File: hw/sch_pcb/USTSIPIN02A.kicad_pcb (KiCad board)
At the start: 2 copper layers, 90.9 x 50.3 mm, 119 parts, among them J1 SM08B-GHS-TB, J2 SD_Card-FPS009-4200-0, J22 HEADER_2x03, J3 SM06B-GHS-TB, J4 USBC_USB4105-GF-A, M1 HOLE, M2 HOLE, M3 HOLE, M4 HOLE, M8 BMI-S-204-F, Q1 BF862, U1 OPA2314, U10 ATMEGA1284P-AU, U11 PCF85263A, U12 MIC5504-3.3YM5, U2 OPA2314, U3 ISL21080DIH312Z-TK 1V25, U4 TS7211, U5 TS5A4594, U6 AT24CS64-SSHM, U7 USBLC6-2SC6, U8 TPS613222ADBV, U9 FT231XQ, Y1 16MHz, Y2 ABS07-120-32.768KHZ-T

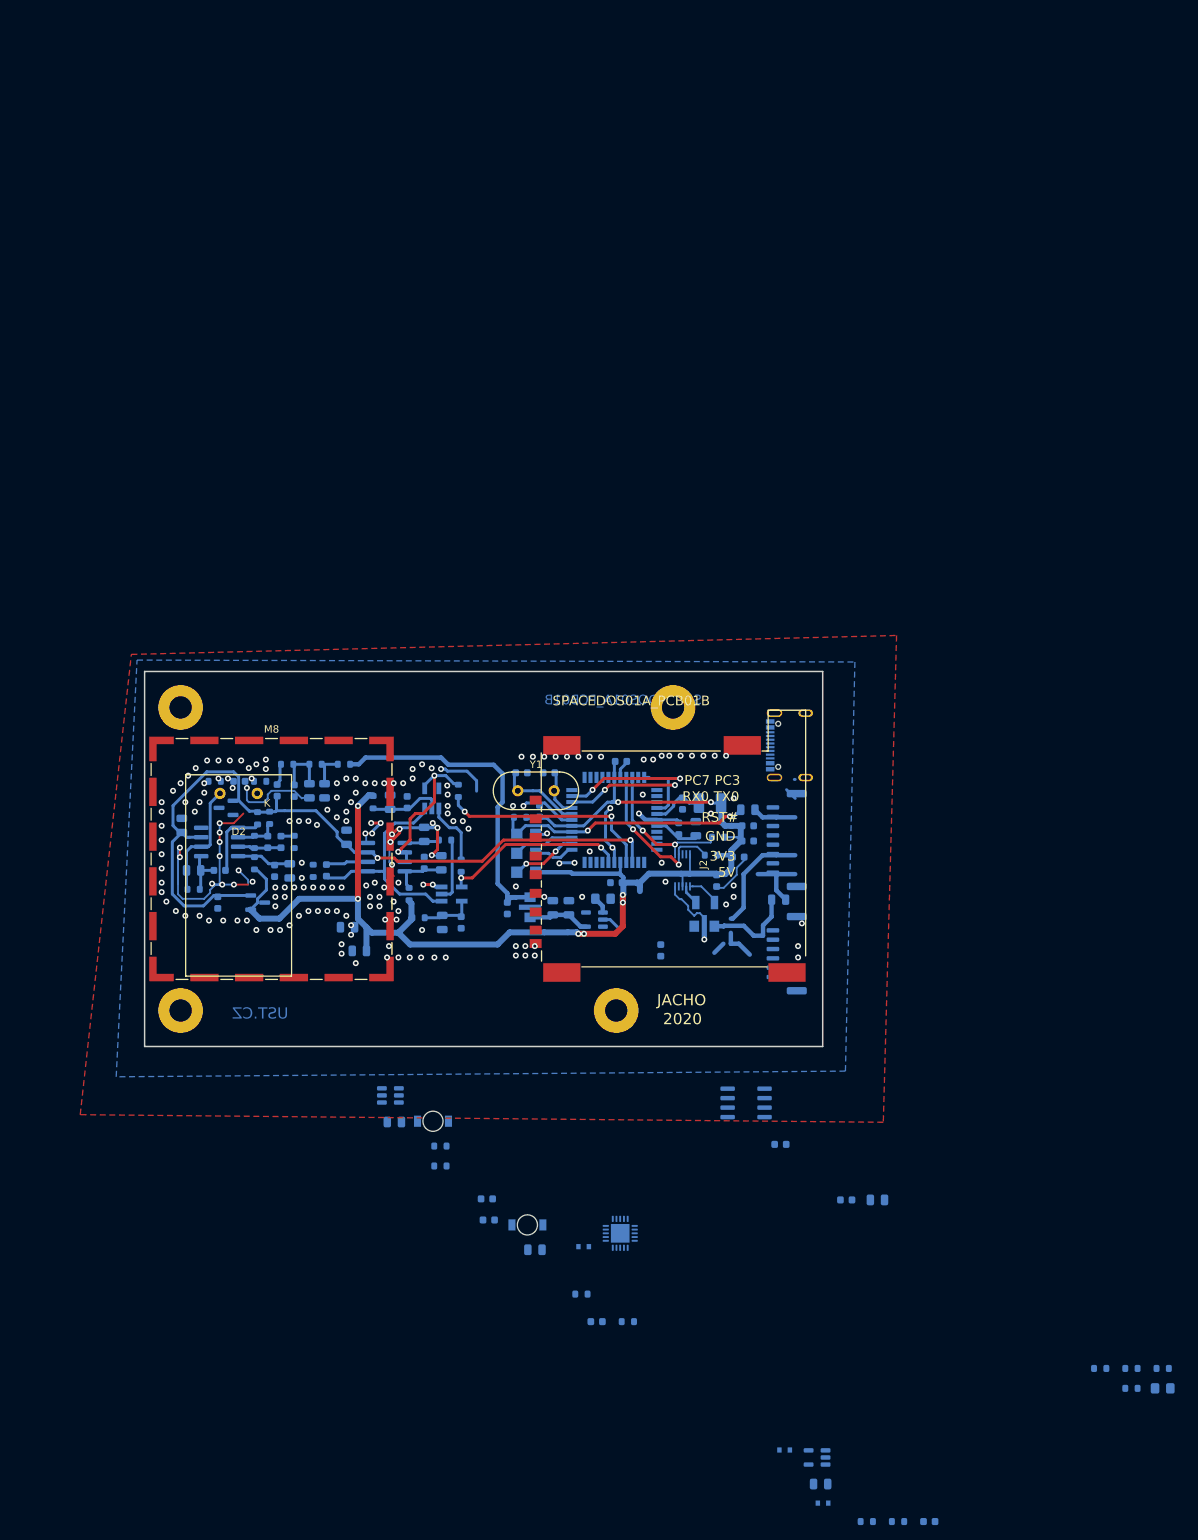
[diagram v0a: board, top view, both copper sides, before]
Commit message: Edit schema and PCB
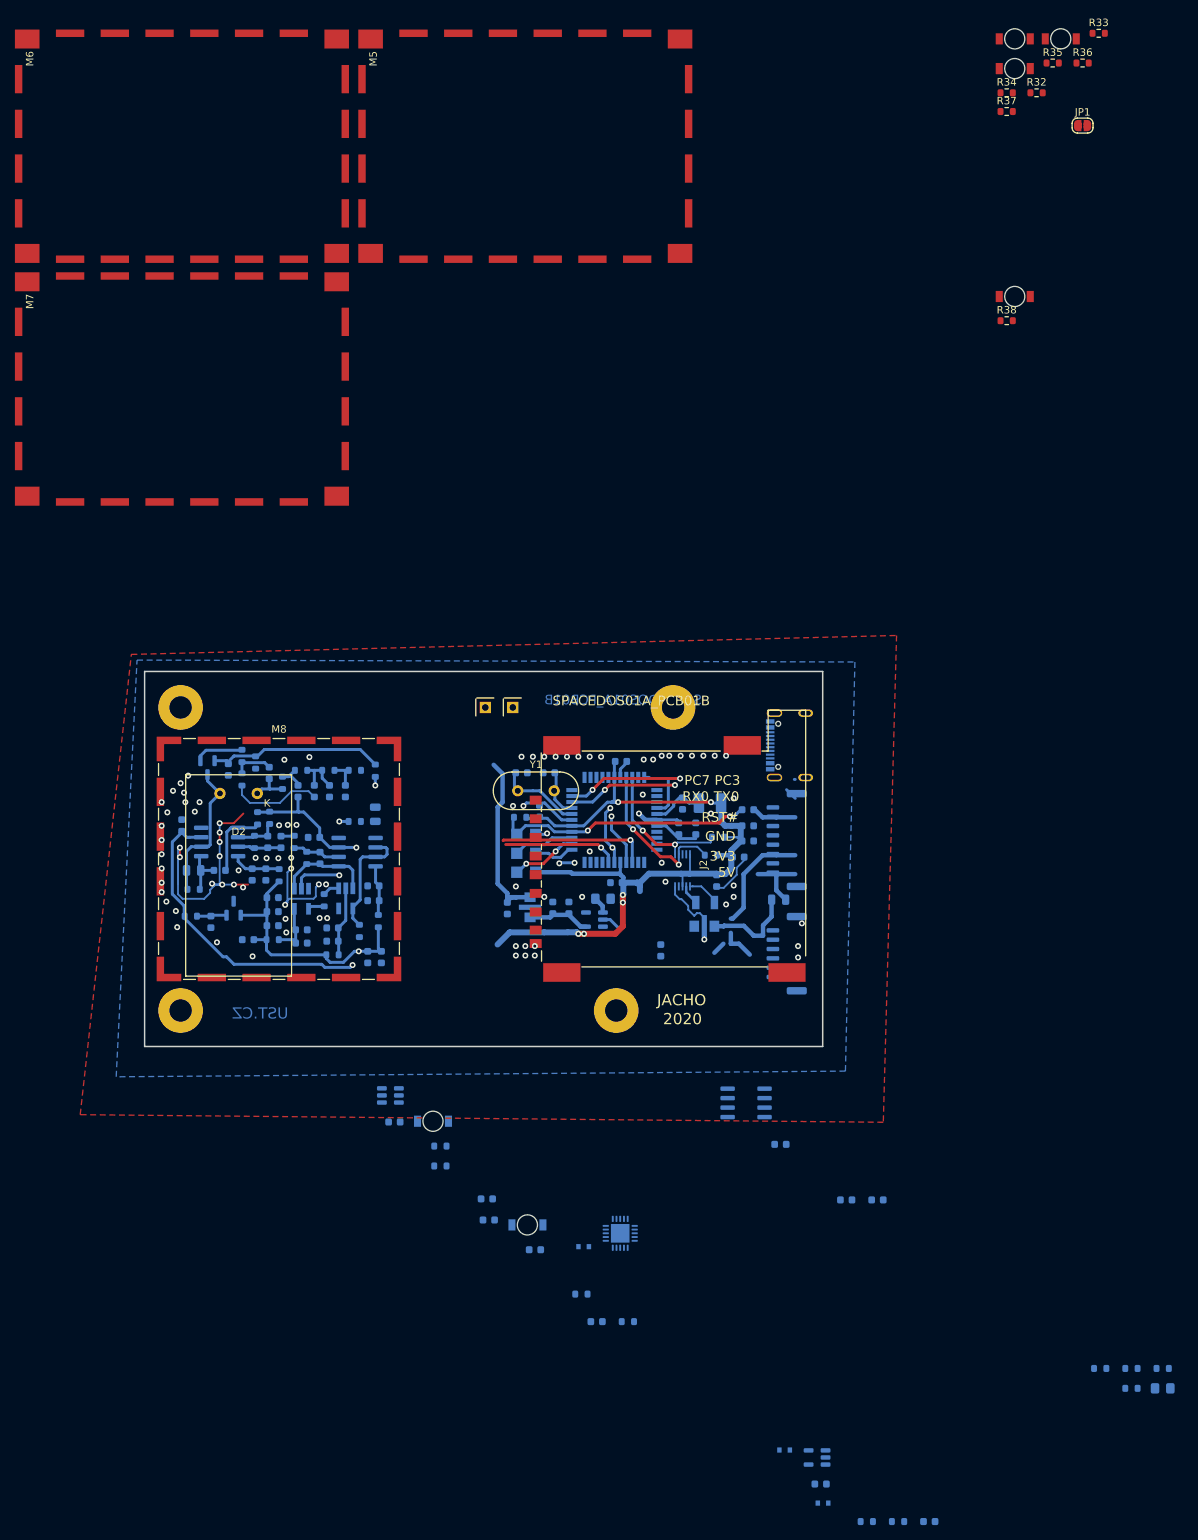
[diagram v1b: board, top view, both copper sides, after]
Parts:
- added C53: 10uF, Resistor_SMD:R_0603_1608Metric, B.Cu at (15.1, -38.3)
- added C55: 10uF, Capacitor_SMD:C_0603_1608Metric, B.Cu at (17.4, -16.5)
- added C56: 10uF, Capacitor_SMD:C_0603_1608Metric, B.Cu at (30.2, -12.2)
- added C57: 10uF, Capacitor_SMD:C_0603_1608Metric, B.Cu at (32.0, -12.2)
- added C58: 10uF, Capacitor_SMD:C_0603_1608Metric, B.Cu at (14.1, -14.6)
- added C59: 100nF, Capacitor_SMD:C_0603_1608Metric, B.Cu at (11.5, -37.4)
- added D10: GREEN, Mlab_D:LED_1206, F.Cu at (116.9, -100.8)
- added D7: RED, Mlab_D:LED_1206, F.Cu at (116.9, -135.4)
- added D8: GREEN, Mlab_D:LED_1206, F.Cu at (123.1, -135.4)
- added D9: GREEN, Mlab_D:LED_1206, F.Cu at (116.9, -131.4)
- added J5: HEADER_1x01, Mlab_Pin_Headers:Straight_1x01, F.Cu at (49.6, -45.7)
- added J6: HEADER_1x01, Mlab_Pin_Headers:Straight_1x01, F.Cu at (45.9, -45.7)
- added JP1: SolderJumper_2_Open, Jumper:SolderJumper-2_P1.3mm_Open_RoundedPad1.0x1.5mm, F.Cu at (126.0, -123.7)
- added M5: BMI-S-210-F, Mlab_Mechanical:BMI-S-210-F, F.Cu at (28.9, -136.6)
- added M6: BMI-S-210-F, Mlab_Mechanical:BMI-S-210-F, F.Cu at (-17.1, -136.6)
- added M7: BMI-S-210-F, Mlab_Mechanical:BMI-S-210-F, F.Cu at (-17.1, -104.1)
- added R32: 100R, Resistor_SMD:R_0603_1608Metric, F.Cu at (119.9, -128.1)
- added R33: 100R, Resistor_SMD:R_0603_1608Metric, F.Cu at (128.2, -136.1)
- added R34: 100R, Resistor_SMD:R_0603_1608Metric, F.Cu at (115.9, -128.1)
- added R35: 180R, Resistor_SMD:R_0603_1608Metric, F.Cu at (122.0, -132.1)
- added R36: 180R, Resistor_SMD:R_0603_1608Metric, F.Cu at (126.0, -132.1)
- added R37: 180R, Resistor_SMD:R_0603_1608Metric, F.Cu at (115.9, -125.6)
- added R38: 180R, Resistor_SMD:R_0603_1608Metric, F.Cu at (115.9, -97.6)
- added R39: 100R, Resistor_SMD:R_0603_1608Metric, B.Cu at (6.45, -17.7)
- added R40: 470R, Resistor_SMD:R_0603_1608Metric, B.Cu at (31.2, -37.2)
- added R41: 0R, Resistor_SMD:R_0603_1608Metric, B.Cu at (13.3, -39.2)
- C1: value 47uF/6V3 -> 10uF; footprint Capacitor_SMD:C_0805_2012Metric -> Capacitor_SMD:C_0603_1608Metric
- C17, C21, C22, C23, C3, C38, C4, C40, C41, C42, C43, C49, C50, C6, C7, C8, C9: footprint Capacitor_SMD:C_0805_2012Metric -> Capacitor_SMD:C_0603_1608Metric
- Q1: value BF862 -> 2SK2394-6
- R17, R18, R24, R25: value 100 -> 100R
- R28, R29: value 270R -> 180R
- moved R1 23.0 mm to (29.1, -15.7)
- moved C14 21.4 mm to (21.3, -15.9), turned to 0 degrees
- moved R4 21.2 mm to (25.5, -12.5), turned to 180 degrees
- moved C8 20.2 mm to (25.5, -14.4), turned to 180 degrees
- moved U5 20.2 mm to (21.3, -20.1), turned to -90 degrees
- moved R5 19.8 mm to (17.4, -14.6)
- moved C13 19.6 mm to (25.5, -16.2), turned to 180 degrees
- moved C9 19.1 mm to (21.3, -14.1), turned to 0 degrees
- moved R12 18.9 mm to (24.3, -19.9)
- moved U4 17.7 mm to (27.2, -20.1), turned to -90 degrees
- moved C4 13.6 mm to (17.4, -20.2), turned to 0 degrees
- moved R13 12.4 mm to (28.4, -30.4), turned to 180 degrees
- moved C7 10.4 mm to (30.9, -19.8), turned to 180 degrees
- moved C1 10.3 mm to (17.4, -18.3), turned to 0 degrees
- moved C12 7.48 mm to (30.9, -21.8), turned to 180 degrees
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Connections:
- C20 pad 1: PA1 -> Net-(C20-Pad1)
- D3 pad 2: +5V -> +3V3
- D4 pad 2: +5V -> +3V3
- J3 pad 2: RX0 -> Net-(J3-Pad2)
- J3 pad 3: TX0 -> Net-(J3-Pad3)
- J3 pad 5: unconnected-(J3-Pad5) -> Net-(J3-Pad5)
- Q1 pad 1: Net-(C37-Pad1) -> Net-(R41-Pad2)
- Q1 pad 2: /VCC1 -> /VCC5
- U10 pad 24: unconnected-(U10-Pad24) -> Net-(R35-Pad2)
- U10 pad 25: unconnected-(U10-Pad25) -> Net-(R36-Pad2)
- U10 pad 26: unconnected-(U10-Pad26) -> Net-(R37-Pad2)
- U3 pad 2: PA1 -> Net-(C20-Pad1)
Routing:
- net +3V3: track 180.7 -> 111.9 mm, vias 10 -> 6
- net POWER_ANALOG_3V3: track 0.00 -> 59.9 mm, vias 0 -> 2
- net GND: track 131.3 -> 105.2 mm, vias 180 -> 92
- net /VCC5: track 0.00 -> 23.8 mm
- net PA0: track 29.1 -> 7.00 mm, vias 2 -> 1
- net +5V: track 44.0 -> 24.1 mm
- net Net-(C18-Pad1): track 30.1 -> 13.0 mm
- net PB0: track 25.1 -> 17.6 mm, vias 2 -> 1
- net Net-(R13-Pad2): track 8.52 -> 15.2 mm, vias 0 -> 2
- net Net-(R12-Pad2): track 8.51 -> 2.27 mm
- net Net-(R41-Pad2): track 0.00 -> 6.23 mm
- net Net-(C37-Pad1): track 0.00 -> 5.44 mm, vias 2 -> 0
- net /K: track 0.00 -> 5.40 mm, vias 1 -> 0
- net Net-(R1-Pad2): track 21.2 -> 15.8 mm, vias 2 -> 0
- net unconnected-(U10-Pad26): track 5.01 -> 0.00 mm
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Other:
- copper layers 2 -> 4
- rule pad_to_mask_clearance: 0 -> 0.2

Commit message: Edit PCB
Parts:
- M8: moved to B.Cu
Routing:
- net Net-(C19-Pad1): track 0.00 -> 4.18 mm
- net GND: vias 92 -> 97

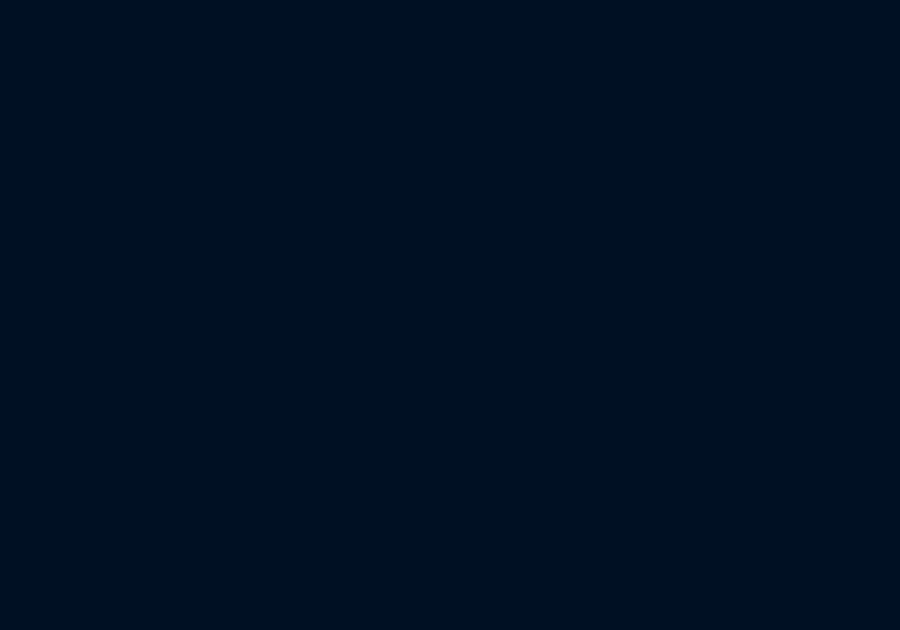
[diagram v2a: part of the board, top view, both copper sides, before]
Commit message: Edit schema and PCB
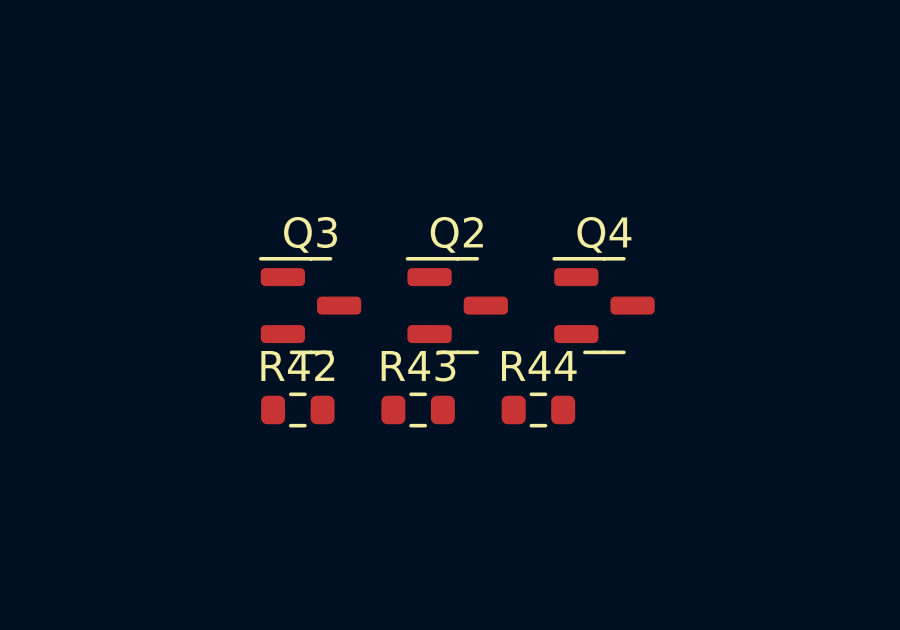
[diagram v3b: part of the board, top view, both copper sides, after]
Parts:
- added Q2: BC817-25, Package_TO_SOT_SMD:SOT-23, F.Cu at (117.0, -7.92)
- added Q3: BC817-25, Package_TO_SOT_SMD:SOT-23, F.Cu at (112.2, -7.92)
- added Q4: BC817-25, Package_TO_SOT_SMD:SOT-23, F.Cu at (121.9, -7.92)
- added R42: 220R, Resistor_SMD:R_0603_1608Metric, F.Cu at (111.7, -4.44)
- added R43: 220R, Resistor_SMD:R_0603_1608Metric, F.Cu at (115.7, -4.44)
- added R44: 220R, Resistor_SMD:R_0603_1608Metric, F.Cu at (119.7, -4.44)
- D7: value RED -> GREEN
- R35, R36, R37: value 180R -> 220R
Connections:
- C29 pad 3: Net-(C29-Pad3) -> Vin
- C41 pad 1: Net-(C29-Pad3) -> Vin
- C46 pad 1: Net-(C29-Pad3) -> Vin
- D7 pad 2: +3V3 -> Vin
- D8 pad 2: +3V3 -> Vin
- D9 pad 2: +3V3 -> Vin
- R35 pad 1: Net-(D7-Pad1) -> /cpu/PC5_D1
- R35 pad 2: Net-(R35-Pad2) -> Net-(Q2-Pad1)
- R36 pad 1: Net-(D8-Pad1) -> Net-(Q2-Pad3)
- R36 pad 2: Net-(R36-Pad2) -> Net-(D7-Pad1)
- R37 pad 1: Net-(D9-Pad1) -> /cpu/PC7_D3
- R37 pad 2: Net-(R37-Pad2) -> Net-(Q3-Pad1)
- U10 pad 24: Net-(R35-Pad2) -> /cpu/PC5_D1
- U10 pad 25: Net-(R36-Pad2) -> /cpu/PC6_D2
- U10 pad 26: Net-(R37-Pad2) -> /cpu/PC7_D3
- U12 pad 1: Net-(C29-Pad3) -> Vin
- U12 pad 3: Net-(C29-Pad3) -> Vin
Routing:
- net Net-(D5-Pad1): track 8.97 -> 0.00 mm
- net GND: track 105.2 -> 114.1 mm
- net RST#: track 5.82 -> 0.00 mm
- net /cpu/EXTINT: track 0.00 -> 5.82 mm
- net Net-(R37-Pad2): track 5.01 -> 0.00 mm
- net /cpu/PC7_D3: track 0.00 -> 5.01 mm

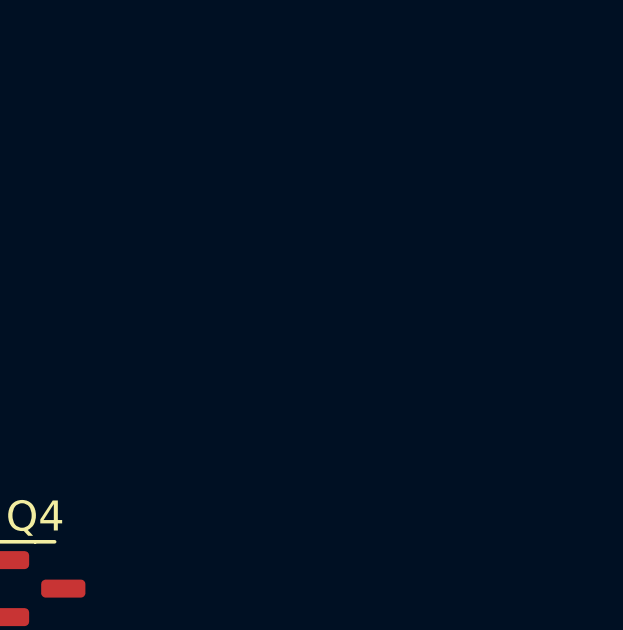
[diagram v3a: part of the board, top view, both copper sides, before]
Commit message: Edit schema and PCB
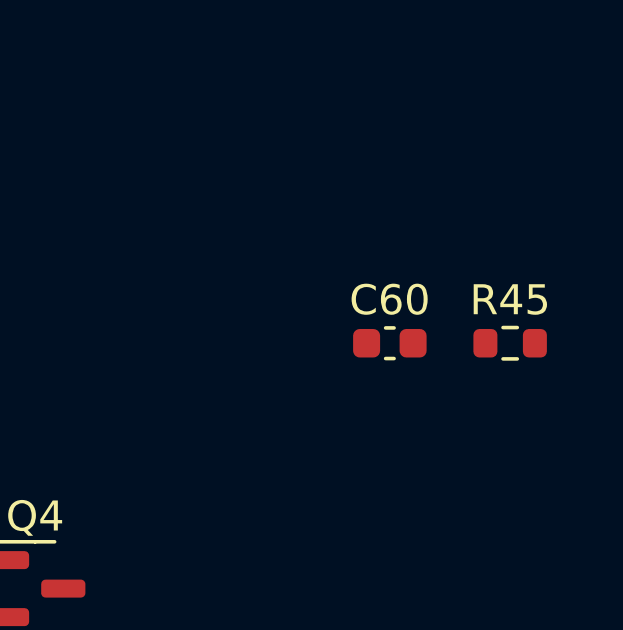
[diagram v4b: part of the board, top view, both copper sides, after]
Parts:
- added C60: 100nF, Capacitor_SMD:C_0603_1608Metric, F.Cu at (133.8, -16.1)
- added R45: 100R, Resistor_SMD:R_0603_1608Metric, F.Cu at (137.8, -16.1)
- C17, C3: value 4u7 -> 1uF
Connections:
- U10 pad 16: POWER_ANALOG_3V3 -> Net-(U10-Pad16)
- U11 pad 3: +3V3 -> Net-(U11-Pad3)
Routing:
- net Net-(D5-Pad1): track 0.00 -> 8.97 mm
- net GND: track 114.1 -> 105.2 mm
- net RST#: track 0.00 -> 5.82 mm
- net /cpu/EXTINT: track 5.82 -> 0.00 mm

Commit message: Editing PCB and schema
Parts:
- removed M5, M6, M7: BMI-S-210-F, Mlab_Mechanical:BMI-S-210-F
- added BT1: KEYS2998, Battery:BatteryHolder_Keystone_2998_1x6.8mm, F.Cu at (43.9, -45.5)
- C22, C25, J22, R17, R18, R24, R25: moved to F.Cu
- C60, JP1, Q2, Q3, Q4, R32, R33, R34, R35, R36, R37, R38, R42, R43, R44, R45: moved to B.Cu
- D10, D7, D8, D9: footprint Mlab_D:LED_1206 -> LED_SMD:LED_1206_3216Metric
- D3, D4: footprint Mlab_D:LED_1206 -> LED_SMD:LED_1206_3216Metric; moved to F.Cu
- moved D7 148.1 mm to (47.0, -4.83), turned to -90 degrees
- moved D8 148.0 mm to (53.3, -4.83), turned to -90 degrees
- moved R36 147.7 mm to (44.2, -9.14), turned to 90 degrees
- moved R35 141.2 mm to (51.8, -9.65), turned to 180 degrees
- moved D9 138.6 mm to (59.9, -5.08), turned to -90 degrees
- moved R37 138.3 mm to (42.9, -8.13), turned to 180 degrees
- moved R33 119.6 mm to (82.3, -25.7)
- moved R32 116.3 mm to (79.5, -19.1), turned to 180 degrees
- moved R17 114.6 mm to (51.8, -35.7), turned to 0 degrees
- moved L2 111.2 mm to (53.8, -28.4)
- moved JP1 111.0 mm to (82.7, -21.6)
- moved R30 110.2 mm to (81.5, -45.0), turned to 90 degrees
- moved R34 109.5 mm to (82.3, -23.9)
- moved R18 108.3 mm to (51.6, -33.4), turned to 0 degrees
- moved R25 106.3 mm to (51.8, -21.0), turned to 0 degrees
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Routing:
- net +3V3: track 111.9 -> 0.00 mm, vias 6 -> 0
- net GND: track 105.2 -> 59.0 mm, vias 97 -> 53
- net /cpu/RST#_P: track 34.6 -> 0.00 mm, vias 2 -> 0
- net +5V: track 24.1 -> 0.00 mm
- net /cpu/PC0: track 21.7 -> 0.00 mm, vias 2 -> 0
- net PA1: track 103.3 -> 83.1 mm, vias 3 -> 2
- net /cpu/PC1: track 19.7 -> 0.00 mm, vias 2 -> 0
- net TX0: track 15.5 -> 0.00 mm, vias 2 -> 0
- net PB0: track 17.6 -> 2.23 mm, vias 1 -> 0
- net /cpu/TX1: track 14.8 -> 0.00 mm
- net RX0: track 14.8 -> 0.00 mm, vias 2 -> 0
- net Net-(C29-Pad1): track 12.5 -> 0.00 mm
- net Net-(C30-Pad1): track 11.1 -> 0.00 mm
- net Net-(D5-Pad1): track 8.97 -> 0.00 mm
- net /cpu/PB6: track 8.97 -> 0.00 mm, vias 2 -> 0
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
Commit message: Edit PCB
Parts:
- moved R29 41.6 mm to (64.3, -9.14), turned to 90 degrees
- moved R30 36.3 mm to (85.6, -8.89)
- moved R31 33.5 mm to (85.6, -6.10)
- moved C45 31.3 mm to (74.2, -10.7)
- moved U7 30.9 mm to (80.8, -8.89)
- moved C60 25.0 mm to (66.3, -27.9)
- moved R43 19.6 mm to (59.2, -7.62), turned to 90 degrees
- moved Q3 18.6 mm to (58.7, -5.08), turned to 0 degrees
- moved D5 17.8 mm to (82.8, -18.3)
- moved R44 15.1 mm to (54.4, -7.68), turned to -90 degrees
- moved Q4 14.9 mm to (53.6, -5.08), turned to 0 degrees
- moved R37 14.0 mm to (56.9, -9.14), turned to -90 degrees
- moved R42 9.67 mm to (51.8, -9.14), turned to -90 degrees
- moved D8 5.92 mm to (59.3, -5.08)
- moved D9 5.69 mm to (54.3, -5.08)
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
